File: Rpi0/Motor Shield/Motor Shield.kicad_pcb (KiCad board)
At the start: 2 copper layers, 29.8 x 64.8 mm, 30 parts, among them J1 Screw_Terminal_01x02, J2 Conn_02x01, J3 Conn_02x01, J4 Screw_Terminal_01x02, J5 Screw_Terminal_01x02, J6 Conn_01x04_Female, J7 Conn_01x04_Female, Q1 Q_PMOS_GDSD, U1 IFX9201SG, U2 IFX9201SG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

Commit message: Added template for pic
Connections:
- net Net-(U3-Pad15) renamed /PIC16LF1509/PWM4
- net Net-(U3-Pad17) renamed /PIC16LF1509/PWM3

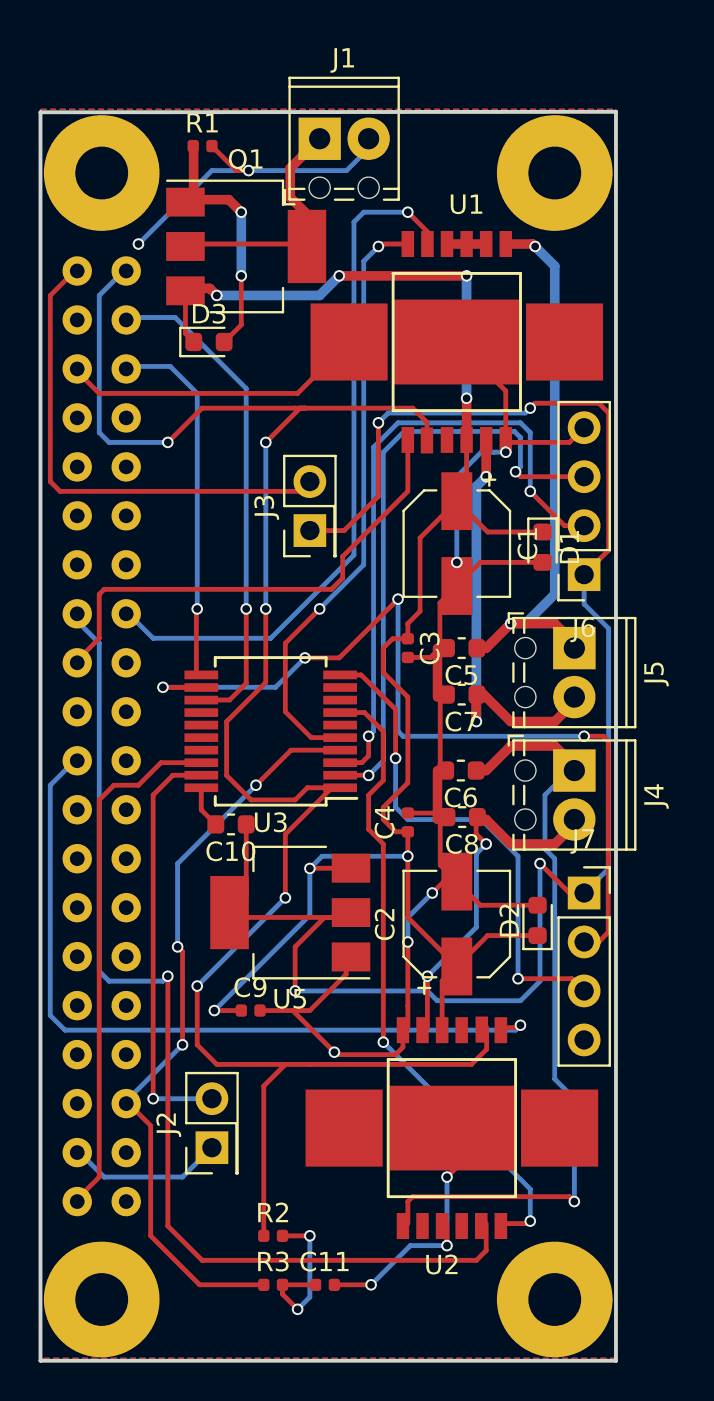
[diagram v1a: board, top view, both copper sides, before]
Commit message: Updated Regulator, Added text, Changed all pins to pic, better 3d view, REV.1 of board
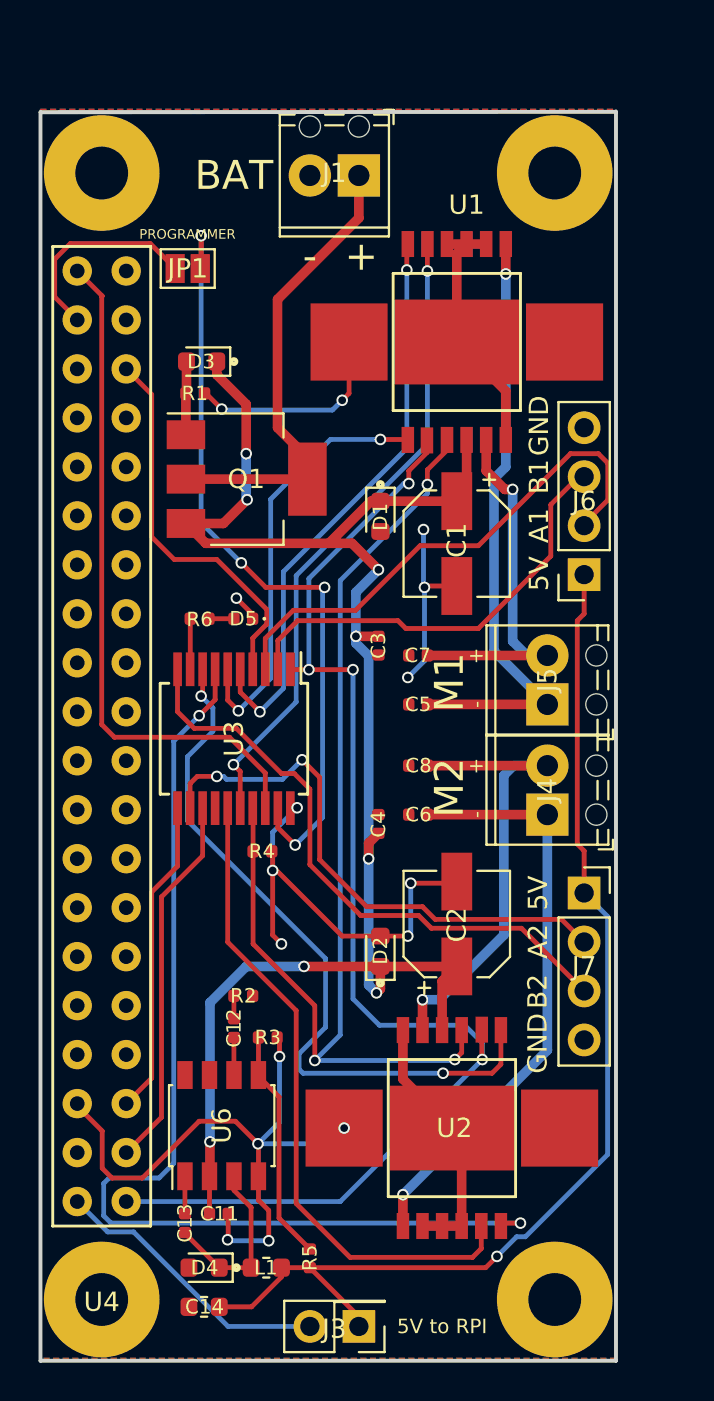
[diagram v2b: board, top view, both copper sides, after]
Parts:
- removed C10: 10uF, Capacitor_SMD:C_0603_1608Metric
- removed C9: 100nF, Capacitor_SMD:C_0402_1005Metric
- removed J2: Conn_02x01, Connector_PinHeader_2.54mm:PinHeader_2x01_P2.54mm_Vertical
- removed U5: LD1117S50TR_SOT223, Package_TO_SOT_SMD:SOT-223-3_TabPin2
- added C12: 2.2nF, Capacitor_SMD:C_0402_1005Metric, F.Cu at (152.3, 117.5)
- added C13: 10nF, Capacitor_SMD:C_0402_1005Metric, F.Cu at (149.7, 127.6)
- added C14: 22uF, Capacitor_SMD:C_0603_1608Metric, F.Cu at (150.7, 132.0)
- added D4: 40V, Diode_SMD:D_0603_1608Metric, F.Cu at (150.7, 129.9)
- added D5: GREEN, LED_SMD:LED_0402_1005Metric, F.Cu at (152.8, 96.3)
- added JP1: SolderJumper_2_Open, Jumper:SolderJumper-2_P1.3mm_Open_Pad1.0x1.5mm, F.Cu at (149.9, 78.1)
- added L1: 15uH, Inductor_SMD:L_0603_1608Metric, F.Cu at (153.9, 129.9)
- added R4: 10k, Resistor_SMD:R_0402_1005Metric, F.Cu at (153.7, 108.3)
- added R5: 28.7k, Resistor_SMD:R_0402_1005Metric, F.Cu at (156.2, 129.4)
- added R6: 50, Resistor_SMD:R_0402_1005Metric, F.Cu at (150.5, 96.3)
- added U6: ACT4060A, Package_SO:SSOP-8_3.95x5.21x3.27mm_P1.27mm, F.Cu at (151.6, 122.6)
- C11: value 1uF -> 10uF
- C5, C6, C7, C8: footprint Capacitor_SMD:C_0603_1608Metric -> Capacitor_SMD:C_0402_1005Metric
- R2: value 10k -> 15k
- R3: value 470 -> 10k
- U4: moved to F.Cu
- moved J3 41.4 mm to (158.8, 133.0), turned to 180 degrees
- moved R1 12.8 mm to (150.3, 84.6)
- moved R3 12.8 mm to (154.0, 118.0)
- moved R2 12.5 mm to (152.8, 115.8)
- moved Q1 12.1 mm to (152.9, 89.0)
- moved D1 8.56 mm to (159.9, 91.0)
- moved D2 8.31 mm to (159.9, 113.5)
- moved C11 6.63 mm to (151.5, 127.1)
- moved U4 5.08 mm to (152.4, 104.9)
- moved C5 3.70 mm to (161.8, 100.7)
- moved C8 3.51 mm to (161.8, 103.9)
- moved J5 3.24 mm to (168.5, 100.7), turned to 90 degrees
- moved C6 3.19 mm to (161.8, 106.4)
- moved C7 3.04 mm to (161.8, 98.2)
- moved J1 2.79 mm to (158.8, 73.3), turned to 180 degrees
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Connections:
- C11 pad 1: Net-(C11-Pad1) -> BAT-PROT+
- R2 pad 1: +3V3 -> Net-(C12-Pad2)
- R2 pad 2: Net-(C11-Pad1) -> BAT-
- R3 pad 1: MCLR -> Net-(R3-Pad1)
- R3 pad 2: Net-(C11-Pad1) -> BAT-
- U1 pad 3: ERROR1 -> ERROR
- U2 pad 3: ERROR2 -> ERROR
- U3 pad 15: /PIC16LF1509/PWM4 -> EN2
- U3 pad 16: Net-(U3-Pad16) -> EN1
- U3 pad 17: /PIC16LF1509/PWM3 -> ERROR
- U3 pad 6: Net-(U3-Pad6) -> DIR1
- U3 pad 8: Net-(U3-Pad8) -> DIR2
- U3 pad 9: Net-(U3-Pad9) -> /PIC16LF1509/Bonus
- U4 pad 15: EN1 -> Net-(U4-Pad15)
- U4 pad 16: EN2 -> Net-(U4-Pad16)
- U4 pad 18: DIR1 -> Net-(U4-Pad18)
- U4 pad 22: DIR2 -> Net-(U4-Pad22)
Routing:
- net ERROR: track 0.00 -> 58.4 mm, vias 0 -> 3
- net +3V3: track 98.2 -> 66.5 mm, vias 5 -> 4
- net +5V: track 86.3 -> 58.7 mm, vias 4 -> 1
- net PWM2: track 33.4 -> 55.1 mm
- net EN2: track 54.8 -> 34.1 mm, vias 1 -> 0
- net Net-(JP1-Pad2): track 21.5 -> 40.7 mm, vias 1 -> 4
- net MCLR: track 38.6 -> 20.2 mm, vias 3 -> 0
- net BAT-: track 123.6 -> 105.3 mm, vias 10 -> 16
- net A2: track 45.2 -> 28.8 mm, vias 4 -> 2
- net Net-(R3-Pad1): track 0.00 -> 12.1 mm
- net BAT+: track 12.9 -> 24.4 mm
- net Net-(J3-Pad2): track 25.5 -> 14.7 mm
- net OUT4: track 40.2 -> 30.7 mm
- net Net-(C13-Pad2): track 0.00 -> 9.32 mm
- net Net-(D3-Pad2): track 13.1 -> 3.81 mm, vias 2 -> 0
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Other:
- board text added: "+"
- board text added: "-"
- board text added: "5V"
- board text added: "5V to RPI"
- board text added: "A1"
- board text added: "A2"
- board text added: "B1"
- board text added: "B2"
- board text added: "BAT"
- board text added: "GND"
- board text added: "M1"
- board text added: "M2"
- board text added: "MOTOR-SHIELD"
- board text added: "PROGRAMMER"
- board text added: "REV.1"
- board text added: "ROB-ORB"
- board text added: "c"

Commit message: Changed footprint
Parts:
- moved U1 0.09 mm to (163.8, 81.8)

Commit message: Added pull-downs to encoders. Rerouted 5V from encoder to real +5V
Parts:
- added 4.7k1: R, Resistors_SMD:R_0402, F.Cu at (168.0, 91.4)
- added 4.7k2: R, Resistors_SMD:R_0402, F.Cu at (167.8, 113.0)
- added 4.7k3: R, Resistors_SMD:R_0402, F.Cu at (167.8, 88.9)
- added 4.7k4: R, Resistors_SMD:R_0402, F.Cu at (167.8, 115.6)
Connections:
- C14 pad 1: +5V -> 5V
- J3 pad 1: +5V -> 5V
- J3 pad 2: Net-(J3-Pad2) -> +5V
- L1 pad 2: +5V -> 5V
- R5 pad 1: +5V -> 5V
- U4 pad 2: Net-(J3-Pad2) -> +5V
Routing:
- net Net-(J3-Pad2): track 14.7 -> 0.00 mm
- net 5V: track 0.00 -> 9.92 mm
- net A1: track 27.3 -> 20.9 mm
- net +5V: track 58.7 -> 64.8 mm, vias 1 -> 0
- net BAT-: track 105.3 -> 110.9 mm, vias 16 -> 18
- net A2: track 28.8 -> 30.9 mm
- net B2: track 31.6 -> 33.7 mm
- net B1: track 22.8 -> 24.5 mm, vias 0 -> 2

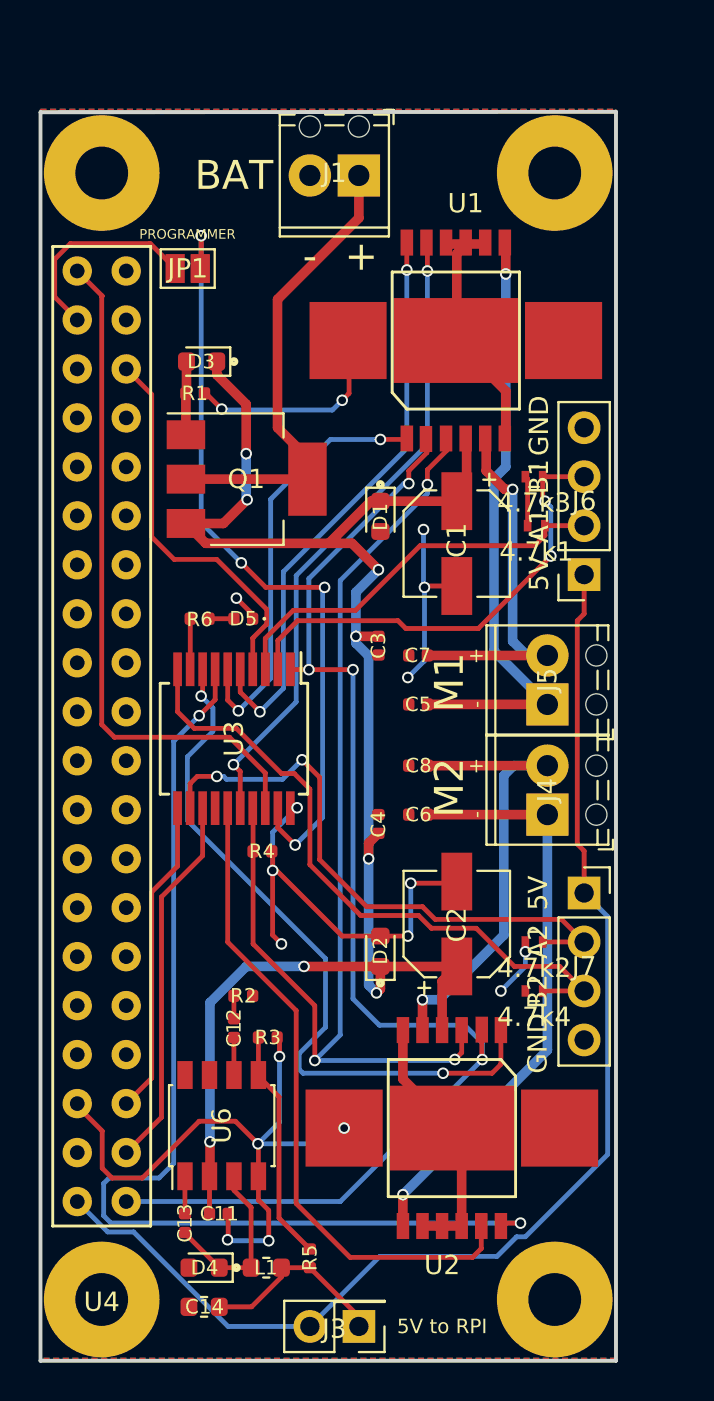
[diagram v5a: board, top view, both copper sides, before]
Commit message: Changed pull down to pull up on the encoders. Recompiled gerbers
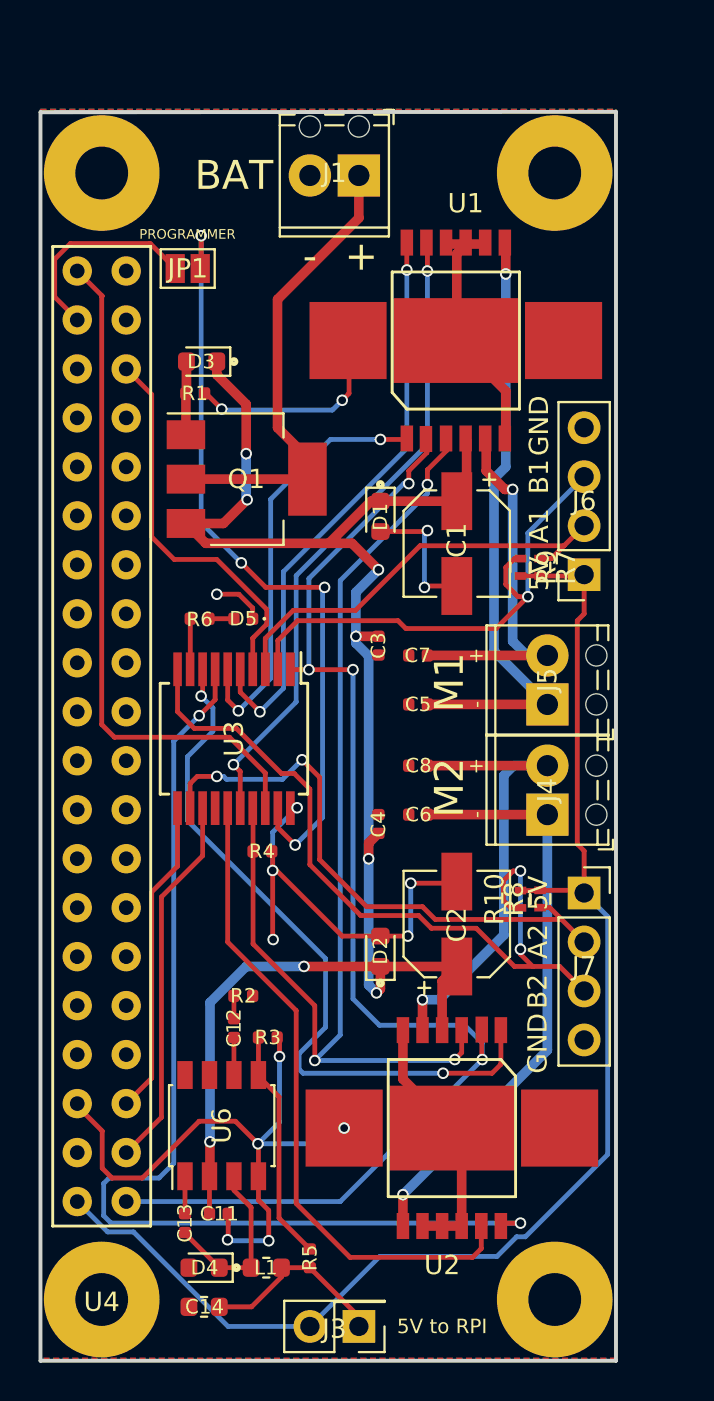
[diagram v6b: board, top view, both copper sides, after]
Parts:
- removed 4.7k1, 4.7k2, 4.7k3, 4.7k4: R, Resistors_SMD:R_0402
- added R10: 1k, Resistors_SMD:R_0402, F.Cu at (167.1, 110.8)
- added R7: 1k, Resistors_SMD:R_0402, F.Cu at (168.1, 93.6)
- added R8: 1k, Resistors_SMD:R_0402, F.Cu at (168.1, 110.8)
- added R9: 1k, Resistors_SMD:R_0402, F.Cu at (167.1, 93.6)
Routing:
- net BAT-: track 110.9 -> 103.9 mm, vias 18 -> 15
- net +5V: track 64.8 -> 71.5 mm
- net B2: track 33.7 -> 40.0 mm, vias 0 -> 2
- net B1: track 24.5 -> 26.7 mm, vias 2 -> 1
- net A1: track 20.9 -> 22.1 mm
- net A2: track 30.9 -> 30.1 mm
